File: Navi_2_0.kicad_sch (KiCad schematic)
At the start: 102 parts, among them J1 USB_B_Micro, J10 BAT-, J2 Conn_01x24_Male, J27 Micro_SD_Card_Det, J9 BAT+, Q1 DMG2301L-7, Q2 TF2310, Q3 DMG2301L-7, Q4 Q_NPN_BEC, Q5 Q_NPN_BEC, Q6 DMG2301L-7, Q7 DMG2301L-7, SW1 SW_Push, SW2 SW_Push, U1 MT3420C, U2 MT3420C, U3 ESP32-WROOM-32, U4 CH340K, U5 L96-M33, U6 LSM303AH, U7 TCN75-3.3

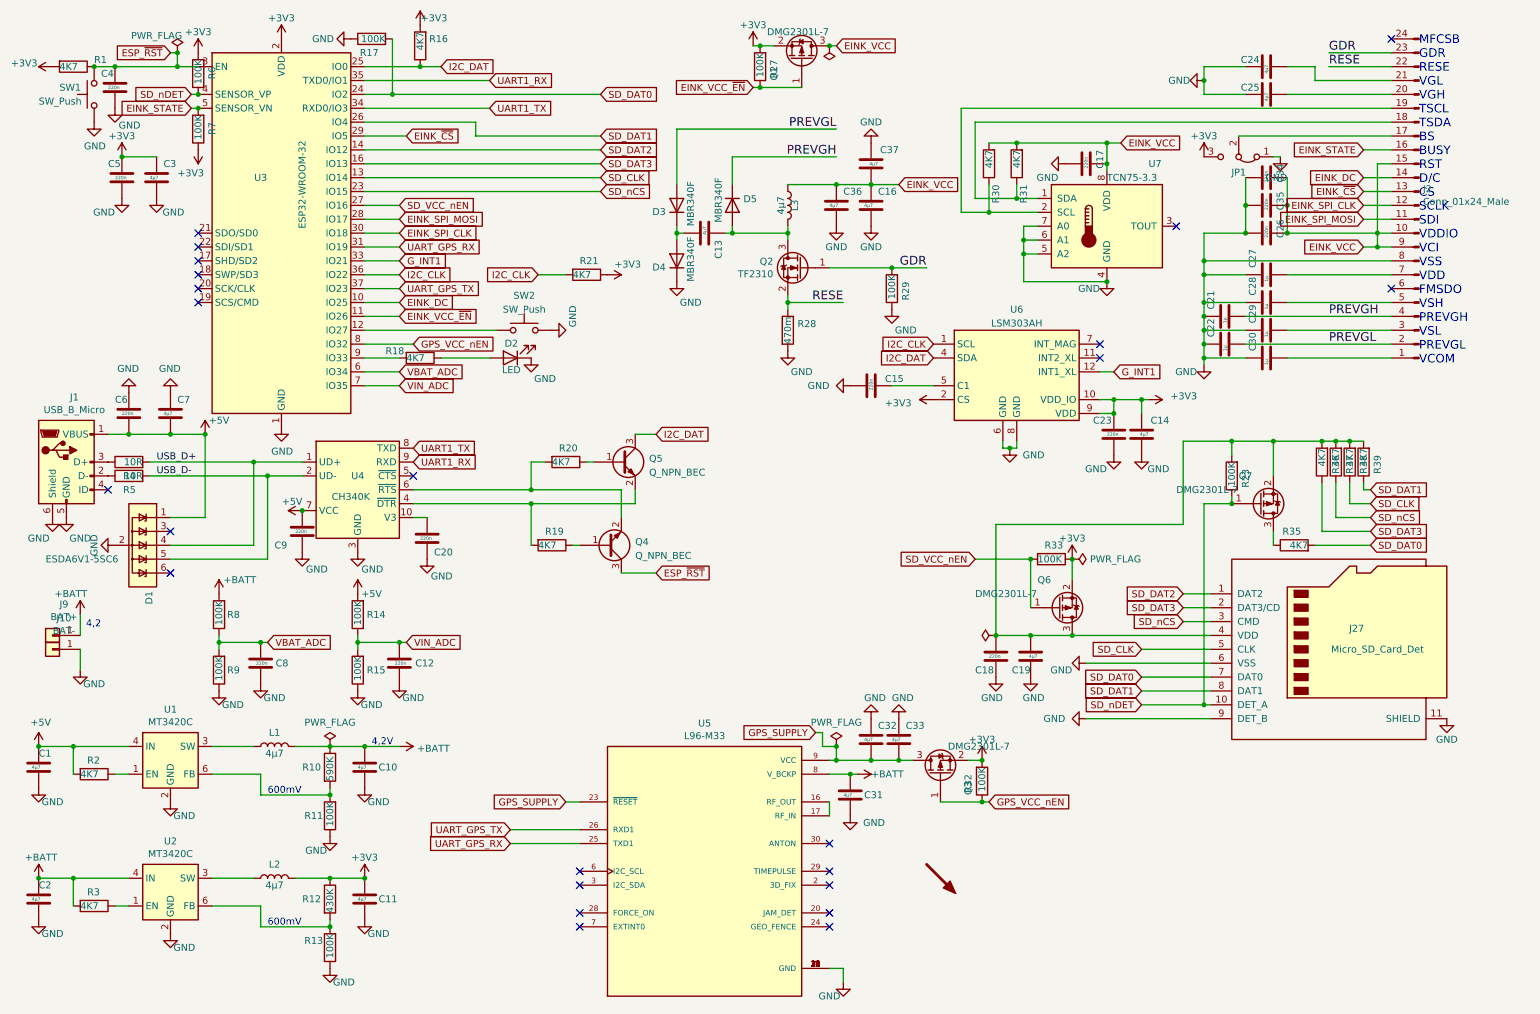
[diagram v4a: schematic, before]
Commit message: changing inductor and connecting reset
Changed Indoctor 4,7µ to 10µ
Connected reset button to 3V3 supply enamble regulator #11
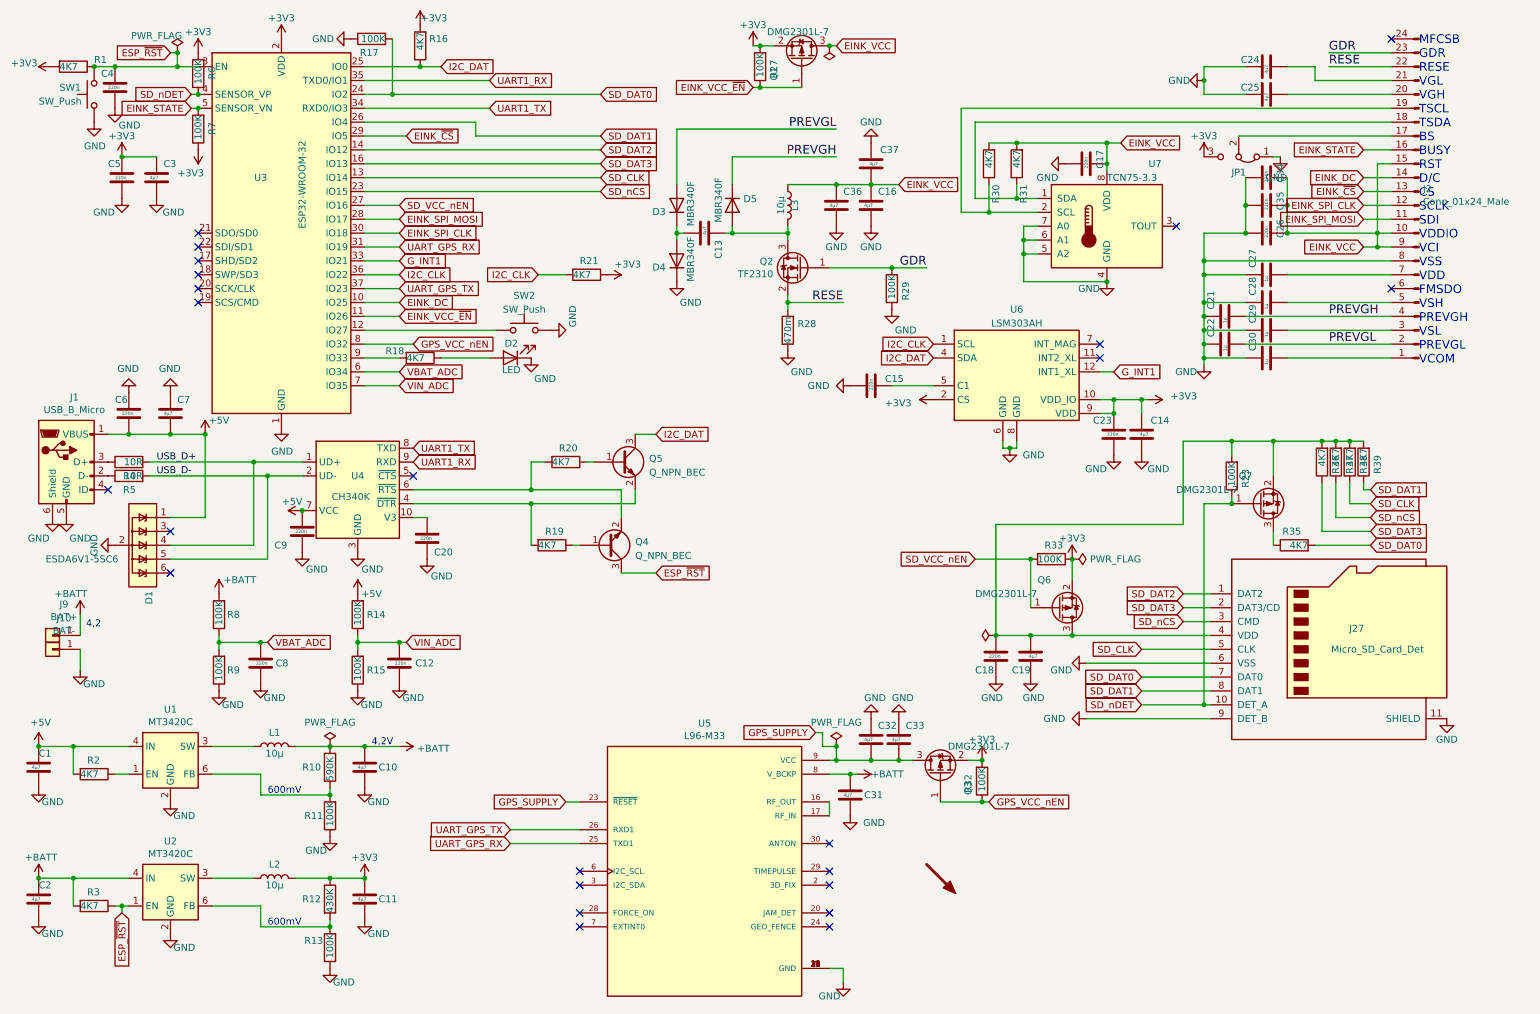
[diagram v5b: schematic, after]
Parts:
- L1, L2, L3: value 4µ7 -> 10µ; footprint Inductor_SMD:L_1008_2520Metric_Pad1.43x2.20mm_HandSolder -> Inductor_SMD:L_Bourns-SRN4018; LCSC C88536 -> C520273
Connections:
- net ESP_~RST: now also R3.1, U2.1 (EN)
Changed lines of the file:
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@@
   (junction (at 31.75 22.86) (diameter 0.9144) (color 0 0 0 0))
   (junction (at 33.02 39.37) (diameter 0.9144) (color 0 0 0 0))
+  (junction (at 33.02 176.53) (diameter 0.9144) (color 0 0 0 0))
   (junction (at 34.29 90.17) (diameter 0.9144) (color 0 0 0 0))
   (junction (at 41.91 90.17) (diameter 0.9144) (color 0 0 0 0))
@@
     (stroke (width 0) (type solid) (color 0 0 0 0))
   )
-  (wire (pts (xy 31.75 176.53) (xy 34.29 176.53))
+  (wire (pts (xy 31.75 176.53) (xy 33.02 176.53))
+    (stroke (width 0) (type solid) (color 0 0 0 0))
+  )
+  (wire (pts (xy 33.02 176.53) (xy 33.02 177.8))
+    (stroke (width 0) (type solid) (color 0 0 0 0))
+  )
+  (wire (pts (xy 33.02 176.53) (xy 34.29 176.53))
     (stroke (width 0) (type solid) (color 0 0 0 0))
   )
@@
     (effects (font (size 1.6002 1.6002)) (justify left bottom))
   )
+  (global_label "ESP_~RST" (shape input) (at 33.02 177.8 270) (fields_autoplaced)
+    (effects (font (size 1.27 1.27)) (justify right))
+    (property "Intersheet References" "${INTERSHEET_REFS}" (id 0) (at 12.7 219.71 0)
+      (effects (font (size 1.27 1.27)) hide)
+    )
+  )
   (global_label "ESP_~RST" (shape input) (at 41.91 20.32 180) (fields_autoplaced)
     (effects (font (size 1.27 1.27)) (justify right))
@@
     (in_bom yes) (on_board yes)
     (property "Reference" "L1" (id 0) (at 60.96 144.78 90))
-    (property "Value" "4µ7" (id 1) (at 60.96 148.59 90))
-    (property "Footprint" "Inductor_SMD:L_1008_2520Metric_Pad1.43x2.20mm_HandSolder" (id 2) (at 60.96 147.32 0)
+    (property "Value" "10µ" (id 1) (at 60.96 148.59 90))
+    (property "Footprint" "Inductor_SMD:L_Bourns-SRN4018" (id 2) (at 60.96 147.32 0)
       (effects (font (size 1.27 1.27)) hide)
     )
@@
       (effects (font (size 1.27 1.27)) hide)
     )
-    (property "LCSC" "C88536" (id 4) (at 60.96 147.32 90)
+    (property "LCSC" "C520273" (id 4) (at 60.96 147.32 90)
       (effects (font (size 1.27 1.27)) hide)
     )
@@
     (in_bom yes) (on_board yes)
     (property "Reference" "L2" (id 0) (at 60.96 168.91 90))
-    (property "Value" "4µ7" (id 1) (at 60.96 172.72 90))
-    (property "Footprint" "Inductor_SMD:L_1008_2520Metric_Pad1.43x2.20mm_HandSolder" (id 2) (at 60.96 171.45 0)
+    (property "Value" "10µ" (id 1) (at 60.96 172.72 90))
+    (property "Footprint" "Inductor_SMD:L_Bourns-SRN4018" (id 2) (at 60.96 171.45 0)
       (effects (font (size 1.27 1.27)) hide)
     )
@@
       (effects (font (size 1.27 1.27)) hide)
     )
-    (property "LCSC" "C88536" (id 4) (at 60.96 171.45 90)
+    (property "LCSC" "C520273" (id 4) (at 60.96 171.45 90)
       (effects (font (size 1.27 1.27)) hide)
     )
@@
     (in_bom yes) (on_board yes)
     (property "Reference" "L3" (id 0) (at 156.21 48.26 90))
-    (property "Value" "4µ7" (id 1) (at 153.67 48.26 90))
-    (property "Footprint" "Inductor_SMD:L_1008_2520Metric_Pad1.43x2.20mm_HandSolder" (id 2) (at 154.94 48.26 0)
+    (property "Value" "10µ" (id 1) (at 153.67 48.26 90))
+    (property "Footprint" "Inductor_SMD:L_Bourns-SRN4018" (id 2) (at 154.94 48.26 0)
       (effects (font (size 1.27 1.27)) hide)
     )
@@
       (effects (font (size 1.27 1.27)) hide)
     )
-    (property "LCSC" "C88536" (id 4) (at 154.94 48.26 90)
+    (property "LCSC" "C520273" (id 4) (at 154.94 48.26 90)
       (effects (font (size 1.27 1.27)) hide)
     )
@@
     )
     (path "/00000000-0000-0000-0000-000060b1caa1"
-      (reference "L1") (unit 1) (value "4µ7") (footprint "Inductor_SMD:L_1008_2520Metric_Pad1.43x2.20mm_HandSolder")
+      (reference "L1") (unit 1) (value "10µ") (footprint "Inductor_SMD:L_Bourns-SRN4018")
     )
     (path "/00000000-0000-0000-0000-000060b20f48"
-      (reference "L2") (unit 1) (value "4µ7") (footprint "Inductor_SMD:L_1008_2520Metric_Pad1.43x2.20mm_HandSolder")
+      (reference "L2") (unit 1) (value "10µ") (footprint "Inductor_SMD:L_Bourns-SRN4018")
     )
     (path "/00000000-0000-0000-0000-0000602c9927"
-      (reference "L3") (unit 1) (value "4µ7") (footprint "Inductor_SMD:L_1008_2520Metric_Pad1.43x2.20mm_HandSolder")
+      (reference "L3") (unit 1) (value "10µ") (footprint "Inductor_SMD:L_Bourns-SRN4018")
     )
     (path "/00000000-0000-0000-0000-0000602ddb35"
